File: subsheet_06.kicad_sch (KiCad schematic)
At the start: 0 parts

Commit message: added todo in schematics
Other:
- note added: "TODO : * Input DC 5~12V (20W), output to 3V3 up to 4/5A * Protect the FPGA board with a diode ? * Reset circuit combine several reset sources (power good, FPGA good, manual reset, PLD/FPGA/Flash reprogramming mode)"
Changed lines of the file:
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@@
     (comment 4 "Original repository :")
   )
+  (text "TODO :\n* Input DC 5~12V (20W), output to 3V3 up to 4/5A\n* Protect the FPGA board with a diode ?\n* Reset circuit combine several reset sources (power good,\nFPGA good, manual reset, PLD/FPGA/Flash reprogramming mode)"
+    (at 25.4 25.4 0)
+    (effects (font (size 1.27 1.27)) (justify left bottom))
+  )
 )

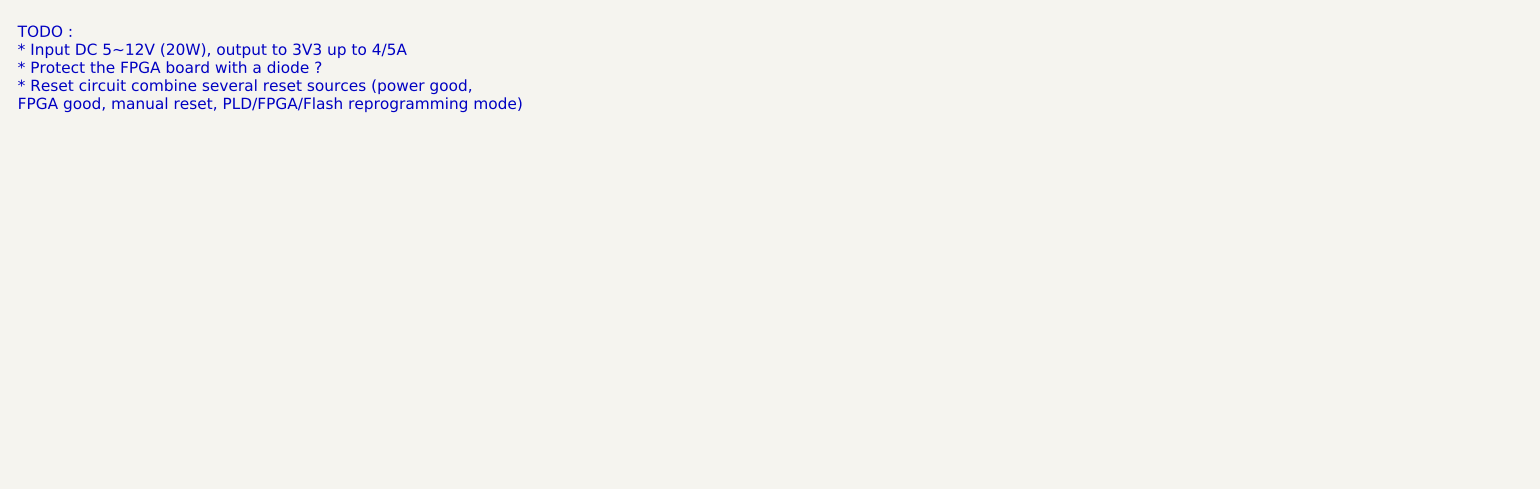
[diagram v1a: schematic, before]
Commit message: Completed CPU (for now), added notes to power supply sheet
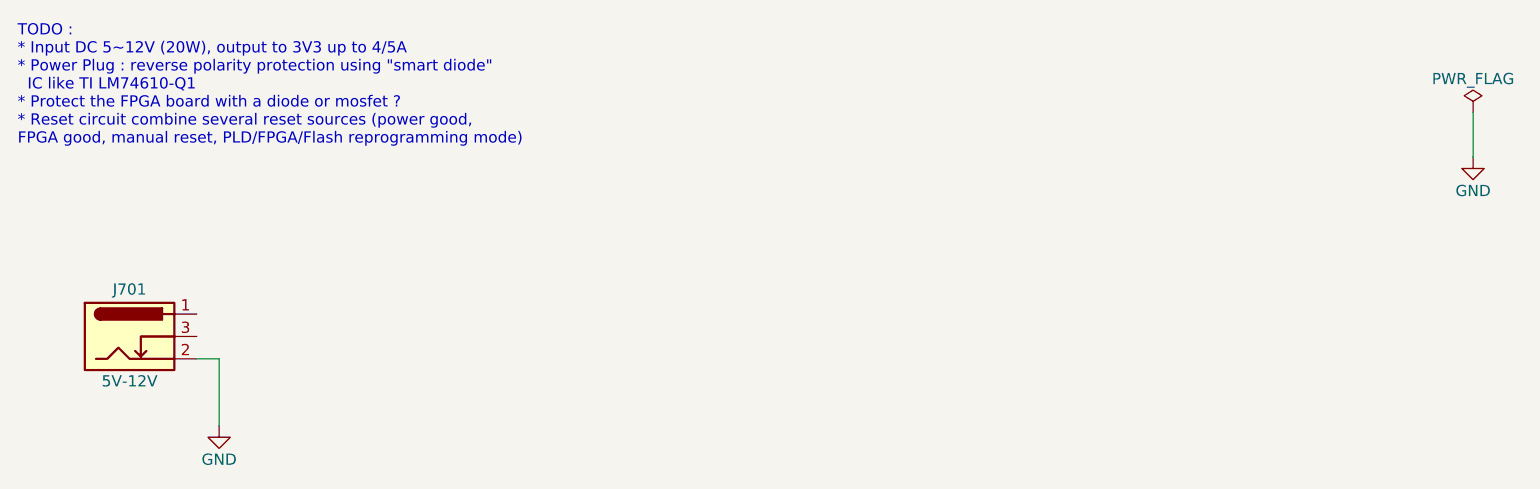
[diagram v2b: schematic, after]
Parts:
- added J701: 5V-12V, symbol Connector:Barrel_Jack_Switch
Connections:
- new net GND: J701.2
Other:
- note added: "TODO : * Input DC 5~12V (20W), output to 3V3 up to 4/5A * Power Plug : reverse polarity protection using "smart diode" IC like TI LM74610-Q1 * Protect the FPGA board with a diode or mosfet ? * Reset circuit combine several reset sources (power good, FPGA good, manual reset, PLD/FPGA/Flash reprogramming mode)"
- note removed: "TODO : * Input DC 5~12V (20W), output to 3V3 up to 4/5A * Protect the FPGA board with a diode ? * Reset circuit combine several reset sources (power good, FPGA good, manual reset, PLD/FPGA/Flash reprogramming mode)"
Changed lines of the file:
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@@
     (comment 4 "Original repository :")
   )
-  (text "TODO :\n* Input DC 5~12V (20W), output to 3V3 up to 4/5A\n* Protect the FPGA board with a diode ?\n* Reset circuit combine several reset sources (power good,\nFPGA good, manual reset, PLD/FPGA/Flash reprogramming mode)"
-    (at 25.4 25.4 0)
+  (wire (pts (xy 45.72 53.34) (xy 48.26 53.34))
+    (stroke (width 0) (type default))
+  )
+  (wire (pts (xy 190.5 25.4) (xy 190.5 30.48))
+    (stroke (width 0) (type default))
+  )
+  (wire (pts (xy 48.26 53.34) (xy 48.26 60.96))
+    (stroke (width 0) (type default))
+  )
+  (text "TODO :\n* Input DC 5~12V (20W), output to 3V3 up to 4/5A\n* Power Plug : reverse polarity protection using \"smart diode\"\n  IC like TI LM74610-Q1\n* Protect the FPGA board with a diode or mosfet ?\n* Reset circuit combine several reset sources (power good,\nFPGA good, manual reset, PLD/FPGA/Flash reprogramming mode)"
+    (at 25.4 29.21 0)
     (effects (font (size 1.27 1.27)) (justify left bottom))
   )
+  (symbol (lib_id "power:GND") (at 48.26 60.96 0) (unit 1)
+    (in_bom yes) (on_board yes) (dnp no)
+    (property "Reference" "#PWR0701" (at 48.26 67.31 0)
+      (effects (font (size 1.27 1.27)) hide)
+    )
+    (property "Value" "GND" (at 48.26 64.77 0)
+      (effects (font (size 1.27 1.27)))
+    )
+    (property "Footprint" "" (at 48.26 60.96 0)
+      (effects (font (size 1.27 1.27)) hide)
+    )
+    (property "Datasheet" "" (at 48.26 60.96 0)
+      (effects (font (size 1.27 1.27)) hide)
+    )
+    (pin "1")
+    (instances
+      (project "ximera-xmr1020-mainboard-by-sporniket"
+        (path "/bfd4e577-e01e-4a6f-987b-f6187790a127/45c7207b-230a-4ebb-a3c5-2a43ee60e3f8"
+          (reference "#PWR0701") (unit 1)
+        )
+      )
+    )
+  )
+  (symbol (lib_id "power:GND") (at 190.5 30.48 0) (unit 1)
+    (in_bom yes) (on_board yes) (dnp no)
+    (property "Reference" "#PWR0702" (at 190.5 36.83 0)
+      (effects (font (size 1.27 1.27)) hide)
+    )
+    (property "Value" "GND" (at 190.5 34.29 0)
+      (effects (font (size 1.27 1.27)))
+    )
+    (property "Footprint" "" (at 190.5 30.48 0)
+      (effects (font (size 1.27 1.27)) hide)
+    )
+    (property "Datasheet" "" (at 190.5 30.48 0)
+      (effects (font (size 1.27 1.27)) hide)
+    )
+    (pin "1")
+    (instances
+      (project "ximera-xmr1020-mainboard-by-sporniket"
+        (path "/bfd4e577-e01e-4a6f-987b-f6187790a127/45c7207b-230a-4ebb-a3c5-2a43ee60e3f8"
+          (reference "#PWR0702") (unit 1)
+        )
+      )
+    )
+  )
+  (symbol (lib_id "power:PWR_FLAG") (at 190.5 25.4 0) (unit 1)
+    (in_bom yes) (on_board yes) (dnp no)
+    (property "Reference" "#FLG0701" (at 190.5 23.495 0)
+      (effects (font (size 1.27 1.27)) hide)
+    )
+    (property "Value" "PWR_FLAG" (at 190.5 21.59 0)
+      (effects (font (size 1.27 1.27)))
+    )
+    (property "Footprint" "" (at 190.5 25.4 0)
+      (effects (font (size 1.27 1.27)) hide)
+    )
+    (property "Datasheet" "~" (at 190.5 25.4 0)
+      (effects (font (size 1.27 1.27)) hide)
+    )
+    (pin "1")
+    (instances
+      (project "ximera-xmr1020-mainboard-by-sporniket"
+        (path "/bfd4e577-e01e-4a6f-987b-f6187790a127/45c7207b-230a-4ebb-a3c5-2a43ee60e3f8"
+          (reference "#FLG0701") (unit 1)
+        )
+      )
+    )
+  )
+  (symbol (lib_id "Connector:Barrel_Jack_Switch") (at 38.1 50.8 0) (unit 1)
+    (in_bom yes) (on_board yes) (dnp no)
+    (property "Reference" "J701" (at 38.1 45.466 0)
+      (effects (font (size 1.27 1.27)))
+    )
+    (property "Value" "5V-12V" (at 38.1 55.88 0)
+      (effects (font (size 1.27 1.27)))
+    )
+    (property "Footprint" "" (at 39.37 51.816 0)
+      (effects (font (size 1.27 1.27)) hide)
+    )
+    (property "Datasheet" "~" (at 39.37 51.816 0)
+      (effects (font (size 1.27 1.27)) hide)
+    )
+    (pin "3")
+    (pin "2")
+    (pin "1")
+    (instances
+      (project "ximera-xmr1020-mainboard-by-sporniket"
+        (path "/bfd4e577-e01e-4a6f-987b-f6187790a127/45c7207b-230a-4ebb-a3c5-2a43ee60e3f8"
+          (reference "J701") (unit 1)
+        )
+      )
+    )
+  )
 )

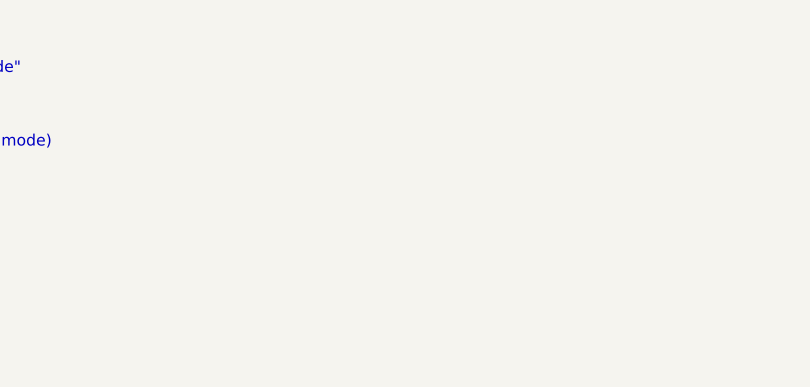
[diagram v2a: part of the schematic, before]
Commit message: Start MFP, with builtin RSVE mod
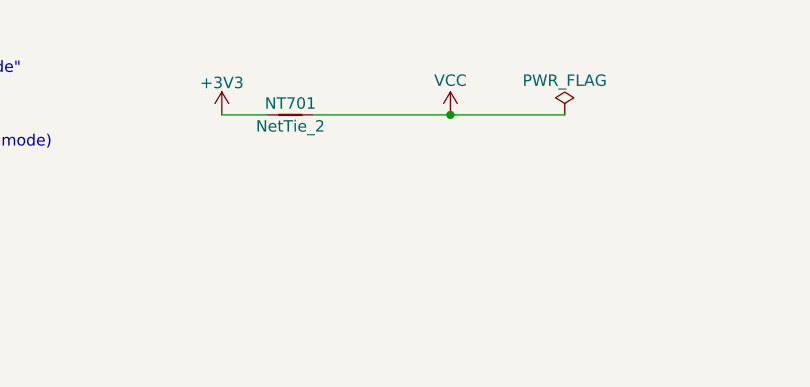
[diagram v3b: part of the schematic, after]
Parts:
- added NT701: NetTie_2, symbol Device:NetTie_2
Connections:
- new net +3V3: NT701.1
- new net VCC: NT701.2
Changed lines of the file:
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@@
     (comment 4 "Original repository :")
   )
+  (junction (at 127 25.4) (diameter 0) (color 0 0 0 0)
+  )
   (wire (pts (xy 45.72 53.34) (xy 48.26 53.34))
+    (stroke (width 0) (type default))
+  )
+  (wire (pts (xy 111.76 25.4) (xy 127 25.4))
+    (stroke (width 0) (type default))
+  )
+  (wire (pts (xy 127 25.4) (xy 139.7 25.4))
     (stroke (width 0) (type default))
   )
@@
   )
   (wire (pts (xy 48.26 53.34) (xy 48.26 60.96))
+    (stroke (width 0) (type default))
+  )
+  (wire (pts (xy 101.6 25.4) (xy 106.68 25.4))
     (stroke (width 0) (type default))
   )
@@
     )
   )
+  (symbol (lib_id "power:PWR_FLAG") (at 139.7 25.4 0) (unit 1)
+    (in_bom yes) (on_board yes) (dnp no)
+    (property "Reference" "#FLG0702" (at 139.7 23.495 0)
+      (effects (font (size 1.27 1.27)) hide)
+    )
+    (property "Value" "PWR_FLAG" (at 139.7 21.59 0)
+      (effects (font (size 1.27 1.27)))
+    )
+    (property "Footprint" "" (at 139.7 25.4 0)
+      (effects (font (size 1.27 1.27)) hide)
+    )
+    (property "Datasheet" "~" (at 139.7 25.4 0)
+      (effects (font (size 1.27 1.27)) hide)
+    )
+    (pin "1")
+    (instances
+      (project "ximera-xmr1020-mainboard-by-sporniket"
+        (path "/bfd4e577-e01e-4a6f-987b-f6187790a127/45c7207b-230a-4ebb-a3c5-2a43ee60e3f8"
+          (reference "#FLG0702") (unit 1)
+        )
+      )
+    )
+  )
+  (symbol (lib_id "power:+3V3") (at 101.6 25.4 0) (unit 1)
+    (in_bom yes) (on_board yes) (dnp no)
+    (property "Reference" "#PWR0703" (at 101.6 29.21 0)
+      (effects (font (size 1.27 1.27)) hide)
+    )
+    (property "Value" "+3V3" (at 101.6 21.844 0)
+      (effects (font (size 1.27 1.27)))
+    )
+    (property "Footprint" "" (at 101.6 25.4 0)
+      (effects (font (size 1.27 1.27)) hide)
+    )
+    (property "Datasheet" "" (at 101.6 25.4 0)
+      (effects (font (size 1.27 1.27)) hide)
+    )
+    (pin "1")
+    (instances
+      (project "ximera-xmr1020-mainboard-by-sporniket"
+        (path "/bfd4e577-e01e-4a6f-987b-f6187790a127/45c7207b-230a-4ebb-a3c5-2a43ee60e3f8"
+          (reference "#PWR0703") (unit 1)
+        )
+      )
+    )
+  )
   (symbol (lib_id "power:GND") (at 190.5 30.48 0) (unit 1)
     (in_bom yes) (on_board yes) (dnp no)
@@
         )
       )
+    )
+  )
+  (symbol (lib_id "power:VCC") (at 127 25.4 0) (unit 1)
+    (in_bom yes) (on_board yes) (dnp no)
+    (property "Reference" "#PWR0704" (at 127 29.21 0)
+      (effects (font (size 1.27 1.27)) hide)
+    )
+    (property "Value" "VCC" (at 127 21.59 0)
+      (effects (font (size 1.27 1.27)))
+    )
+    (property "Footprint" "" (at 127 25.4 0)
+      (effects (font (size 1.27 1.27)) hide)
+    )
+    (property "Datasheet" "" (at 127 25.4 0)
+      (effects (font (size 1.27 1.27)) hide)
+    )
+    (pin "1")
+    (instances
+      (project "ximera-xmr1020-mainboard-by-sporniket"
+        (path "/bfd4e577-e01e-4a6f-987b-f6187790a127/45c7207b-230a-4ebb-a3c5-2a43ee60e3f8"
+          (reference "#PWR0704") (unit 1)
+        )
+      )
+    )
+  )
+  (symbol (lib_id "Device:NetTie_2") (at 109.22 25.4 0) (unit 1)
+    (in_bom no) (on_board yes) (dnp no)
+    (property "Reference" "NT701" (at 109.22 24.13 0)
+      (effects (font (size 1.27 1.27)))
+    )
+    (property "Value" "NetTie_2" (at 109.22 26.67 0)
+      (effects (font (size 1.27 1.27)))
+    )
+    (property "Footprint" "" (at 109.22 25.4 0)
+      (effects (font (size 1.27 1.27)) hide)
+    )
+    (property "Datasheet" "~" (at 109.22 25.4 0)
+      (effects (font (size 1.27 1.27)) hide)
+    )
+    (pin "2")
+    (pin "1")
+    (instances
+      (project "ximera-xmr1020-mainboard-by-sporniket"
+        (path "/bfd4e577-e01e-4a6f-987b-f6187790a127/45c7207b-230a-4ebb-a3c5-2a43ee60e3f8"
+          (reference "NT701") (unit 1)
+        )
+      )

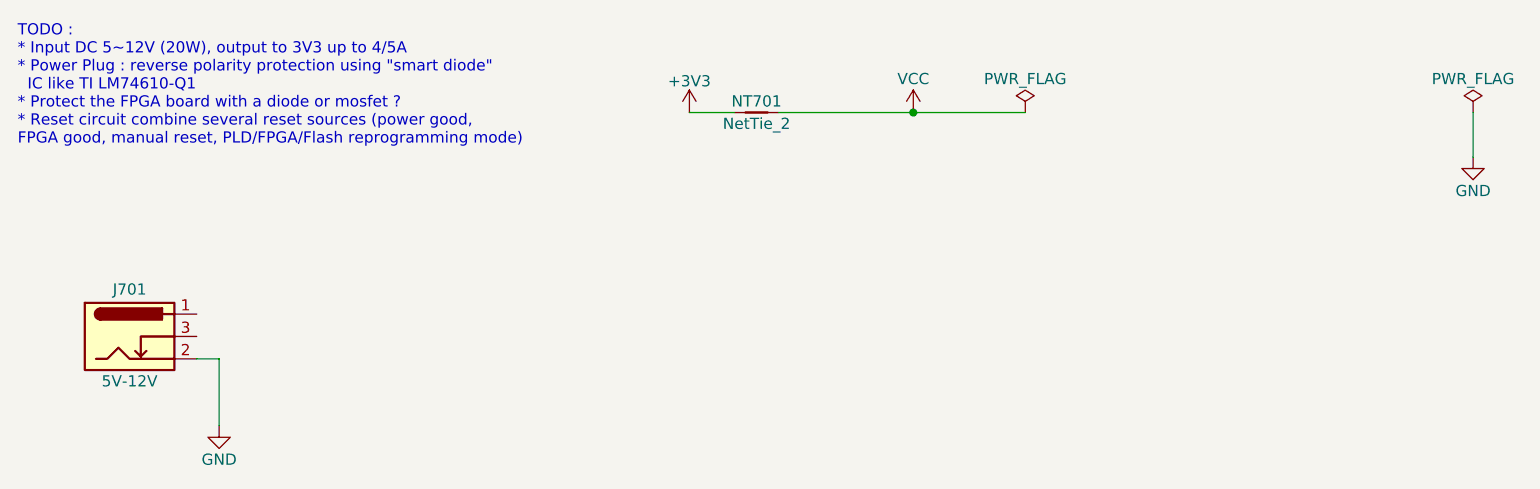
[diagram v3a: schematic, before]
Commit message: added notes for the power supply to make
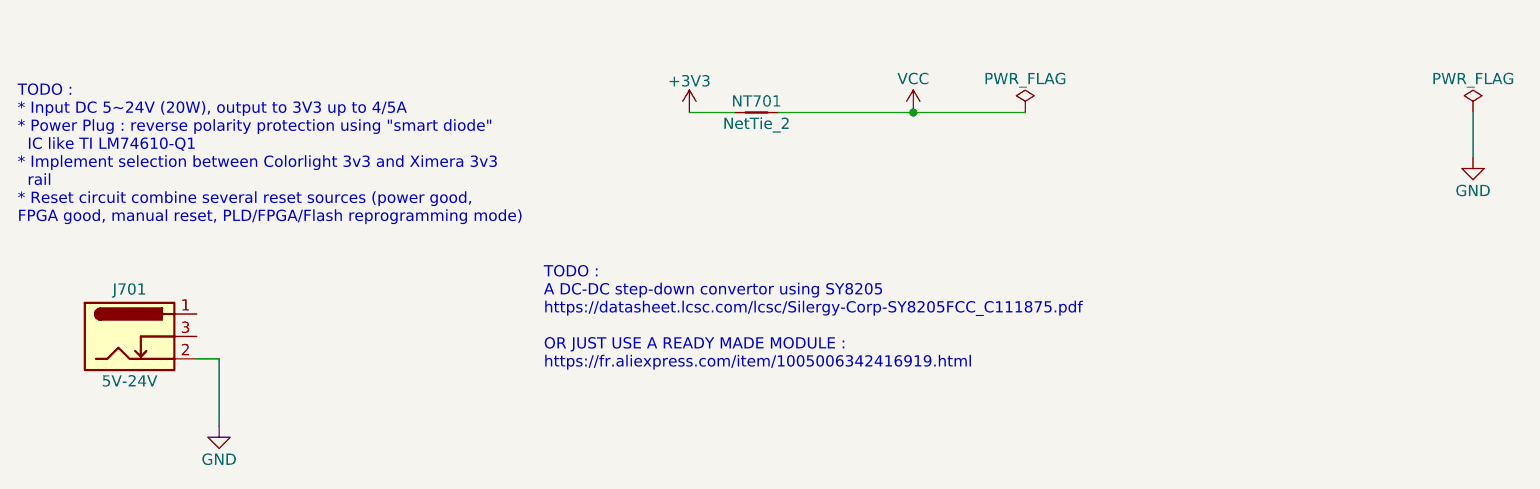
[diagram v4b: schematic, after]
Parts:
- J701: value 5V-12V -> 5V-24V
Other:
- note added: "TODO : * Input DC 5~24V (20W), output to 3V3 up to 4/5A * Power Plug : reverse polarity protection using "smart diode" IC like TI LM74610-Q1 * Implement selection between Colorlight 3v3 and Ximera 3v3 rail * Reset circuit combine several reset sources (power good, FPGA good, manual reset, PLD/FPGA/Flash reprogramming mode)"
- note added: "TODO : A DC-DC step-down convertor using SY8205 https://datasheet.lcsc.com/lcsc/Silergy-Corp-SY8205FCC_C111875.pdf OR JUST USE A READY MADE MODULE : https://fr.aliexpress.com/item/1005006342416919.html"
- note removed: "TODO : * Input DC 5~12V (20W), output to 3V3 up to 4/5A * Power Plug : reverse polarity protection using "smart diode" IC like TI LM74610-Q1 * Protect the FPGA board with a diode or mosfet ? * Reset circuit combine several reset sources (power good, FPGA good, manual reset, PLD/FPGA/Flash reprogramming mode)"
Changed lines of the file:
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@@
     (stroke (width 0) (type default))
   )
-  (text "TODO :\n* Input DC 5~12V (20W), output to 3V3 up to 4/5A\n* Power Plug : reverse polarity protection using \"smart diode\"\n  IC like TI LM74610-Q1\n* Protect the FPGA board with a diode or mosfet ?\n* Reset circuit combine several reset sources (power good,\nFPGA good, manual reset, PLD/FPGA/Flash reprogramming mode)"
-    (at 25.4 29.21 0)
+  (text "TODO : \nA DC-DC step-down convertor using SY8205\nhttps://datasheet.lcsc.com/lcsc/Silergy-Corp-SY8205FCC_C111875.pdf\n\nOR JUST USE A READY MADE MODULE : \nhttps://fr.aliexpress.com/item/1005006342416919.html"
+    (at 85.09 54.61 0)
+    (effects (font (size 1.27 1.27)) (justify left bottom))
+  )
+  (text "TODO :\n* Input DC 5~24V (20W), output to 3V3 up to 4/5A\n* Power Plug : reverse polarity protection using \"smart diode\"\n  IC like TI LM74610-Q1\n* Implement selection between Colorlight 3v3 and Ximera 3v3\n  rail\n* Reset circuit combine several reset sources (power good,\nFPGA good, manual reset, PLD/FPGA/Flash reprogramming mode)"
+    (at 25.4 38.1 0)
     (effects (font (size 1.27 1.27)) (justify left bottom))
   )
@@
       (effects (font (size 1.27 1.27)))
     )
-    (property "Value" "5V-12V" (at 38.1 55.88 0)
+    (property "Value" "5V-24V" (at 38.1 55.88 0)
       (effects (font (size 1.27 1.27)))
     )
